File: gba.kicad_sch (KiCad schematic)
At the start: 16 parts, among them IC1 STM32MP157AAB3, IC7 S40FC004C1B2C00000, SW1 SW_MEC_5G, SW2 SW_MEC_5G

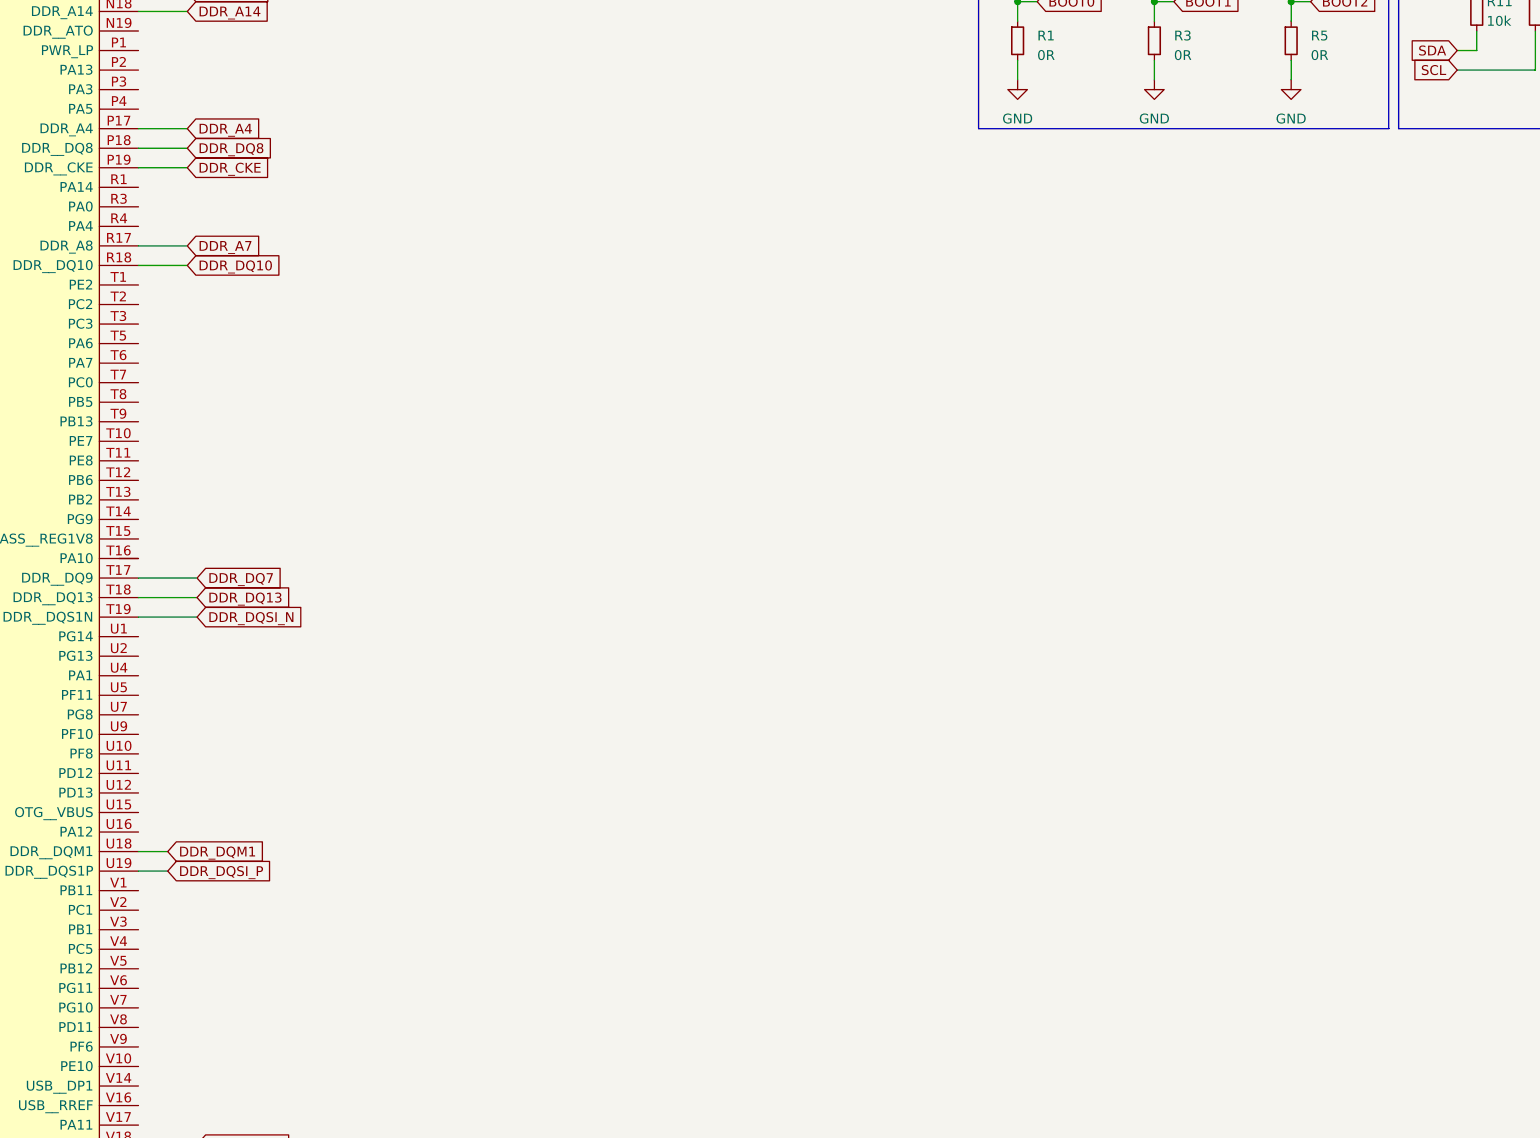
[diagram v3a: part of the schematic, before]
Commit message: Add Uart to MPU
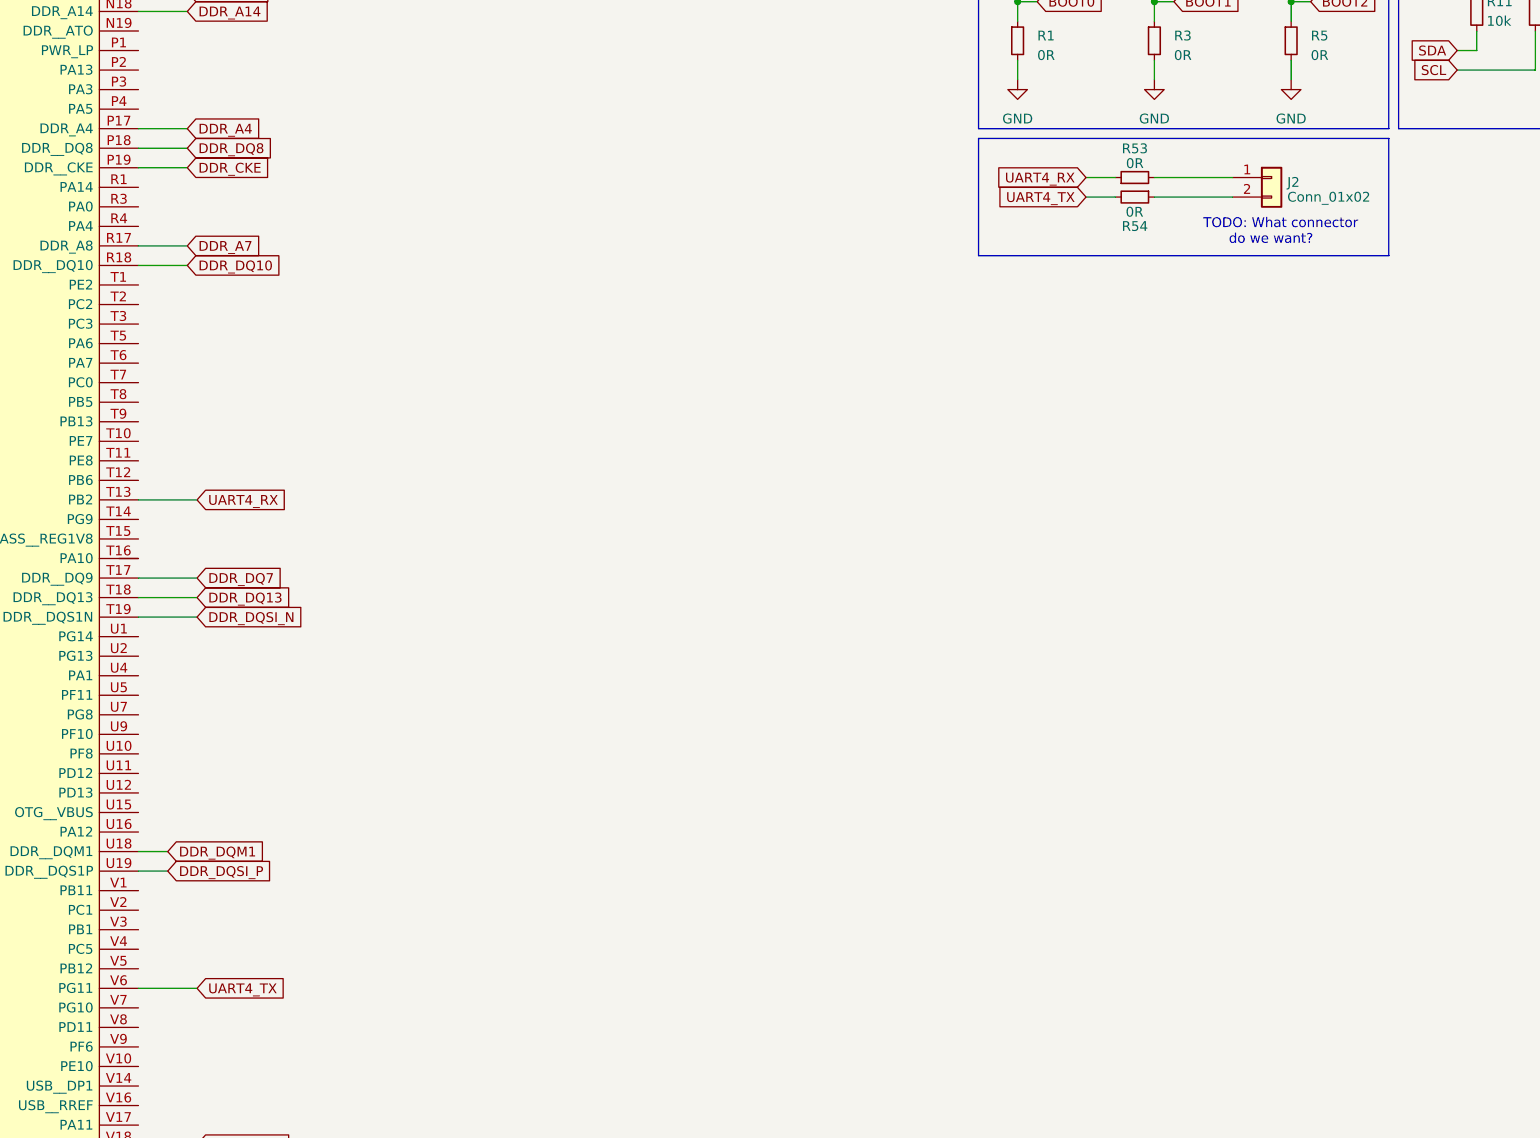
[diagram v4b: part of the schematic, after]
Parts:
- added J2: Conn_01x02, symbol Connector_Generic:Conn_01x02
- added R53, R54: 0R, symbol Device:R_Small
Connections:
- net UART4_RX: now reaches IC1.T13 (PB2)
- net UART4_RX: now also R53.1
- net UART4_TX: now reaches IC1.V6 (PG11)
- net UART4_TX: now also R54.2
- new net: J2.1 (Pin_1), R53.2
- new net: J2.2 (Pin_2), R54.1
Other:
- note added: "TODO: What connector do we want?"
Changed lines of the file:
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@@
+    (stroke (width 0) (type default))
+  )
+  (wire (pts (xy 271.78 107.95) (xy 281.94 107.95))
+    (stroke (width 0) (type default))
+  )
+  (wire (pts (xy 262.89 105.41) (xy 266.7 105.41))
     (stroke (width 0) (type default))
   )
@@
     (stroke (width 0) (type default))
   )
+  (wire (pts (xy 271.78 105.41) (xy 281.94 105.41))
+    (stroke (width 0) (type default))
+  )
   (wire (pts (xy 83.82 63.5) (xy 81.28 63.5))
     (stroke (width 0) (type default))
@@
     (stroke (width 0) (type default))
   )
+  (wire (pts (xy 262.89 107.95) (xy 266.7 107.95))
+    (stroke (width 0) (type default))
+  )
   (wire (pts (xy 384.81 59.69) (xy 384.81 62.23))
     (stroke (width 0) (type default))
@@
     (stroke (width 0) (type default))
   )
+  (wire (pts (xy 139.7 147.32) (xy 147.32 147.32))
+    (stroke (width 0) (type default))
+  )
   (wire (pts (xy 139.7 76.2) (xy 146.05 76.2))
     (stroke (width 0) (type default))
@@
     (stroke (width 0) (type default))
   )
+  (wire (pts (xy 139.7 210.82) (xy 147.32 210.82))
+    (stroke (width 0) (type default))
+  )
   (wire (pts (xy 384.81 46.99) (xy 384.81 49.53))
     (stroke (width 0) (type default))
@@
   (wire (pts (xy 311.15 91.44) (xy 321.31 91.44))
     (stroke (width 0) (type default))
+  )
+  (rectangle (start 248.92 100.33) (end 302.26 115.57)
+    (stroke (width 0) (type default))
+    (fill (type none))
   )
   (text "BOOT Selection" (at 250.19 60.96 0)
@@
   )
   (text "NRST + opt buttons" (at 279.4 34.29 0)
+    (effects (font (size 1.27 1.27)) (justify left bottom))
+  )
+  (text "TODO: What connector\n      do we want?" (at 278.13 114.3 0)
     (effects (font (size 1.27 1.27)) (justify left bottom))
   )
@@
     )
   )
+  (global_label "UART4_RX" (shape input) (at 147.32 147.32 0) (fields_autoplaced)
+    (effects (font (size 1.27 1.27)) (justify left))
+    (property "Intersheetrefs" "${INTERSHEET_REFS}" (at 159.5391 147.32 0)
+      (effects (font (size 1.27 1.27)) (justify left) hide)
+    )
+  )
   (global_label "BOOT0" (shape input) (at 256.54 82.55 0) (fields_autoplaced)
     (effects (font (size 1.27 1.27)) (justify left))
@@
     )
   )
+  (global_label "UART4_RX" (shape input) (at 262.89 105.41 180) (fields_autoplaced)
+    (effects (font (size 1.27 1.27)) (justify right))
+    (property "Intersheetrefs" "${INTERSHEET_REFS}" (at 250.6709 105.41 0)
+      (effects (font (size 1.27 1.27)) (justify right) hide)
+    )
+  )
   (global_label "DDR_BA2" (shape input) (at 146.05 38.1 0) (fields_autoplaced)
     (effects (font (size 1.27 1.27)) (justify left))
@@
     )
   )
+  (global_label "UART4_TX" (shape input) (at 147.32 210.82 0) (fields_autoplaced)
+    (effects (font (size 1.27 1.27)) (justify left))
+    (property "Intersheetrefs" "${INTERSHEET_REFS}" (at 159.2367 210.82 0)
+      (effects (font (size 1.27 1.27)) (justify left) hide)
+    )
+  )
   (global_label "DDR_A14" (shape input) (at 146.05 83.82 0) (fields_autoplaced)
     (effects (font (size 1.27 1.27)) (justify left))
@@
   (global_label "DDR_DQ0" (shape input) (at 74.93 109.22 180) (fields_autoplaced)
     (effects (font (size 1.27 1.27)) (justify right))
+  )
+  (global_label "UART4_TX" (shape input) (at 262.89 107.95 180) (fields_autoplaced)
+    (effects (font (size 1.27 1.27)) (justify right))
+    (property "Intersheetrefs" "${INTERSHEET_REFS}" (at 250.9733 107.95 0)
+      (effects (font (size 1.27 1.27)) (justify right) hide)
+    )
   )
   (global_label "DDR_A1" (shape input) (at 146.05 71.12 0) (fields_autoplaced)
@@
         (path "/017c50c6-333c-4d31-ad5a-278994a09b14"
           (reference "#PWR05") (unit 1)
+        )
+      )
+    )
+  )
+  (symbol (lib_id "Connector_Generic:Conn_01x02") (at 287.02 105.41 0) (unit 1)
+    (in_bom yes) (on_board yes) (dnp no) (fields_autoplaced)
+    (property "Reference" "J2" (at 289.052 106.0363 0)
+      (effects (font (size 1.27 1.27)) (justify left))
+    )
+    (property "Value" "Conn_01x02" (at 289.052 107.9573 0)
+      (effects (font (size 1.27 1.27)) (justify left))
+    )
+    (property "Footprint" "" (at 287.02 105.41 0)
+      (effects (font (size 1.27 1.27)) hide)
+    )
+    (property "Datasheet" "~" (at 287.02 105.41 0)
+      (effects (font (size 1.27 1.27)) hide)
+    )
+    (pin "1")
+    (pin "2")
+    (instances
+      (project "gba"
+        (path "/017c50c6-333c-4d31-ad5a-278994a09b14"
+          (reference "J2") (unit 1)
         )
       )
@@
     )
   )
+  (symbol (lib_id "Device:R_Small") (at 269.24 107.95 270) (unit 1)
+    (in_bom yes) (on_board yes) (dnp no)
+    (property "Reference" "R54" (at 269.24 111.76 90)
+      (effects (font (size 1.27 1.27)))
+    )
+    (property "Value" "0R" (at 269.1999 109.9072 90)
+      (effects (font (size 1.27 1.27)))
+    )
+    (property "Footprint" "" (at 269.24 107.95 0)
+      (effects (font (size 1.27 1.27)) hide)
+    )
+    (property "Datasheet" "~" (at 269.24 107.95 0)
+      (effects (font (size 1.27 1.27)) hide)
+    )
+    (property "MFN" "" (at 269.24 107.95 0)
+      (effects (font (size 1.27 1.27)) hide)
+    )
+    (pin "1")
+    (pin "2")
+    (instances
+      (project "gba"
+        (path "/017c50c6-333c-4d31-ad5a-278994a09b14"
+          (reference "R54") (unit 1)
+        )
+      )
+    )
+  )
   (symbol (lib_id "Device:R_Small") (at 313.69 83.82 0) (mirror y) (unit 1)
     (in_bom yes) (on_board yes) (dnp no)
@@
         )
       )
+    )
+  )
+  (symbol (lib_id "Device:R_Small") (at 269.24 105.41 90) (unit 1)
+    (in_bom yes) (on_board yes) (dnp no) (fields_autoplaced)
+    (property "Reference" "R53" (at 269.24 101.6635 90)
+      (effects (font (size 1.27 1.27)))
+    )
+    (property "Value" "0R" (at 269.24 103.5845 90)
+      (effects (font (size 1.27 1.27)))
+    )
+    (property "Footprint" "" (at 269.24 105.41 0)
+      (effects (font (size 1.27 1.27)) hide)
+    )
+    (property "Datasheet" "~" (at 269.24 105.41 0)
+      (effects (font (size 1.27 1.27)) hide)
+    )
+    (property "MFN" "" (at 269.24 105.41 0)
+      (effects (font (size 1.27 1.27)) hide)
+    )
+    (pin "1")
+    (pin "2")
+    (instances
+      (project "gba"
+        (path "/017c50c6-333c-4d31-ad5a-278994a09b14"
+          (reference "R53") (unit 1)
+        )
+      )

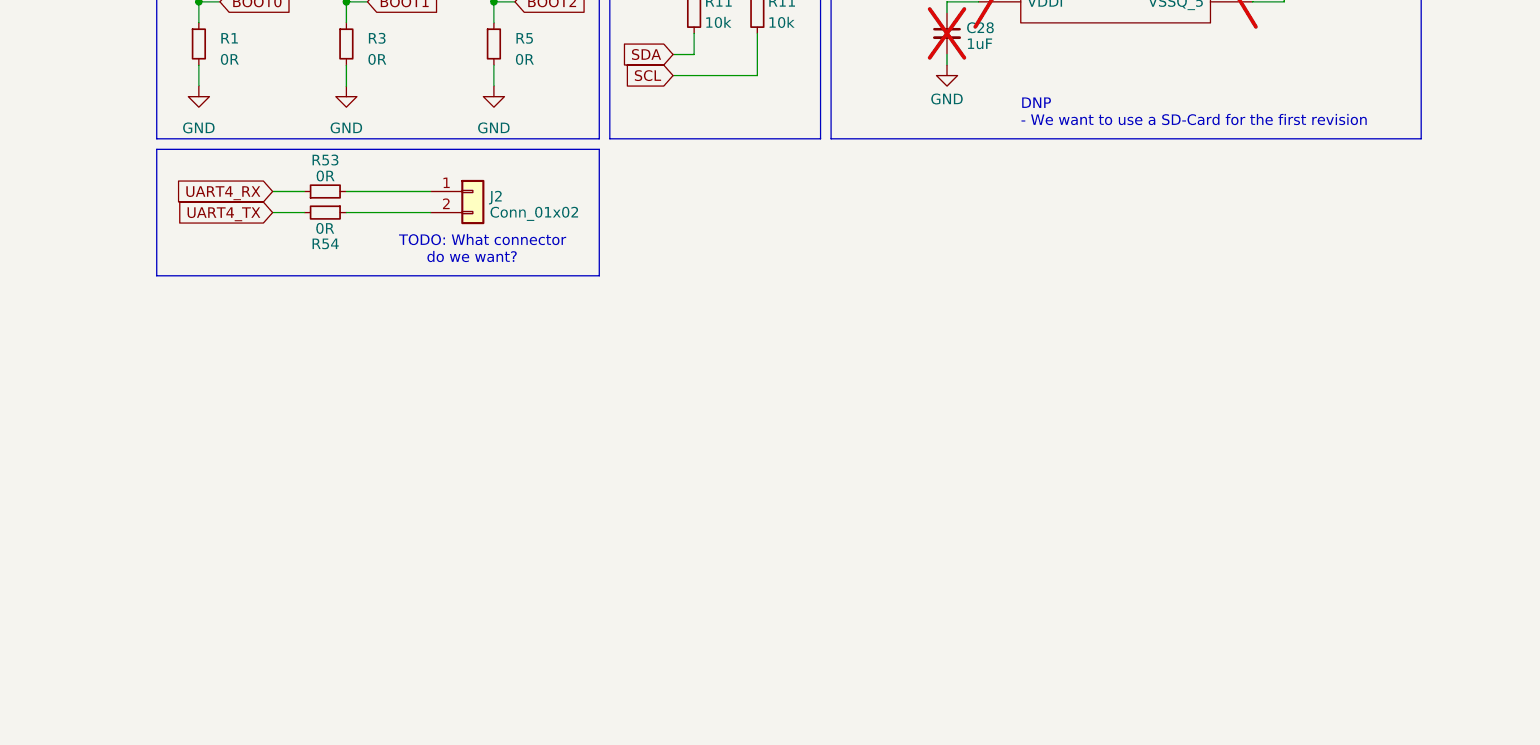
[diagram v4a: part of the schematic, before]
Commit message: Add SDcard Adapter
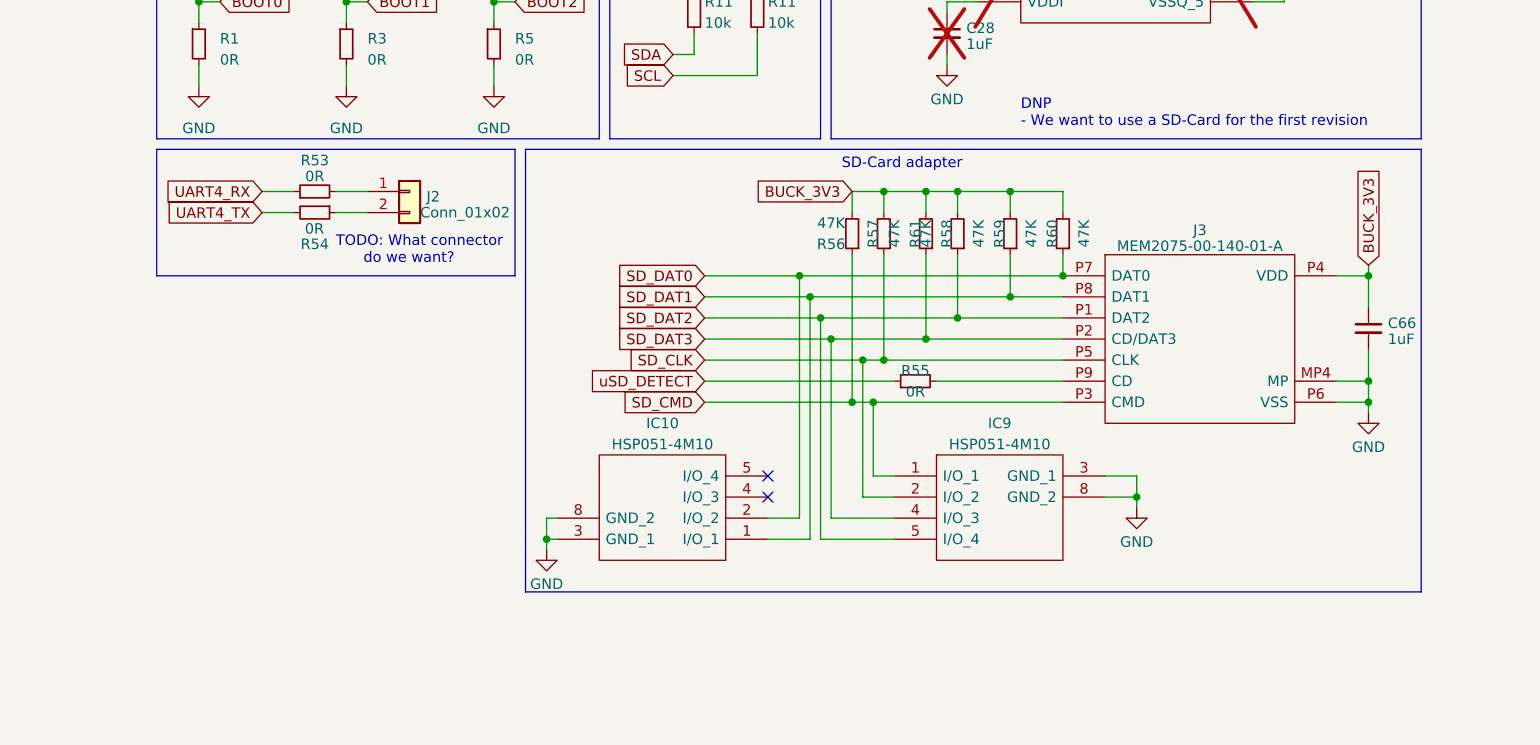
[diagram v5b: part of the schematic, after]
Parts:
- added C66: 1uF, symbol Device:C_Small
- added IC10, IC9: HSP051-4M10, HSP0514M10, symbol ARMband:HSP051-4M10
- added J3: MEM2075-00-140-01-A, MEM20750014001A, symbol ARMband:MEM2075-00-140-01-A
- added R55: 0R, symbol Device:R_Small
- added R56, R57, R58, R59, R60, R61: 47K, symbol Device:R_Small
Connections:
- net BUCK_3V3: now also C66.1, J3.P4 (VDD), R56.2, R57.2, R58.2, R59.2, R60.2, R61.2
- net GND: now also C66.2, IC10.3 (GND_1), IC10.8 (GND_2), IC9.3 (GND_1), IC9.8 (GND_2), J3.MP1, J3.MP2, J3.MP3, J3.MP4 (MP), J3.P6 (VSS)
- net SD_CLK: now also IC9.2 (I/O_2), J3.P5 (CLK), R57.1
- net SD_CMD: now also IC9.1 (I/O_1), J3.P3 (CMD), R56.1
- net SD_DAT0: now also IC10.2 (I/O_2), J3.P7 (DAT0), R60.1
- net SD_DAT1: now also IC10.1 (I/O_1), J3.P8 (DAT1), R59.1
- net SD_DAT2: now also IC9.5 (I/O_4), J3.P1 (DAT2), R58.1
- net SD_DAT3: now also IC9.4 (I/O_3), J3.P2 (CD/DAT3), R61.1
- new net: J3.P9 (CD), R55.2
- new net: IC9.10 (INTERNAL_LY_NOT_CONNECTED_4), IC9.6 (INTERNAL_LY_NOT_CONNECTED_1), IC9.7 (INTERNAL_LY_NOT_CONNECTED_2), IC9.9 (INTERNAL_LY_NOT_CONNECTED_3)
- new net: IC10.10 (INTERNAL_LY_NOT_CONNECTED_4), IC10.6 (INTERNAL_LY_NOT_CONNECTED_1), IC10.7 (INTERNAL_LY_NOT_CONNECTED_2), IC10.9 (INTERNAL_LY_NOT_CONNECTED_3)
- new net uSD_DETECT: R55.1
- no-connect marks 5 -> 7
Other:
- note added: "SD-Card adapter"
- moved on the sheet: J2, R53, R54
